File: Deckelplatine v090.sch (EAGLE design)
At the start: 67 parts, among them IC1 MAX1487EESA+, IC2 74HCT595D, IC3 74HCT595D, IC4 74HCT595D, IC5 74HCT595D, IC6 74HCT595D, J1 52808-2570, Q1 BC846BSMD, Q2 BC846BSMD, U1 LM2676S, X1 236-404, X2 233-502

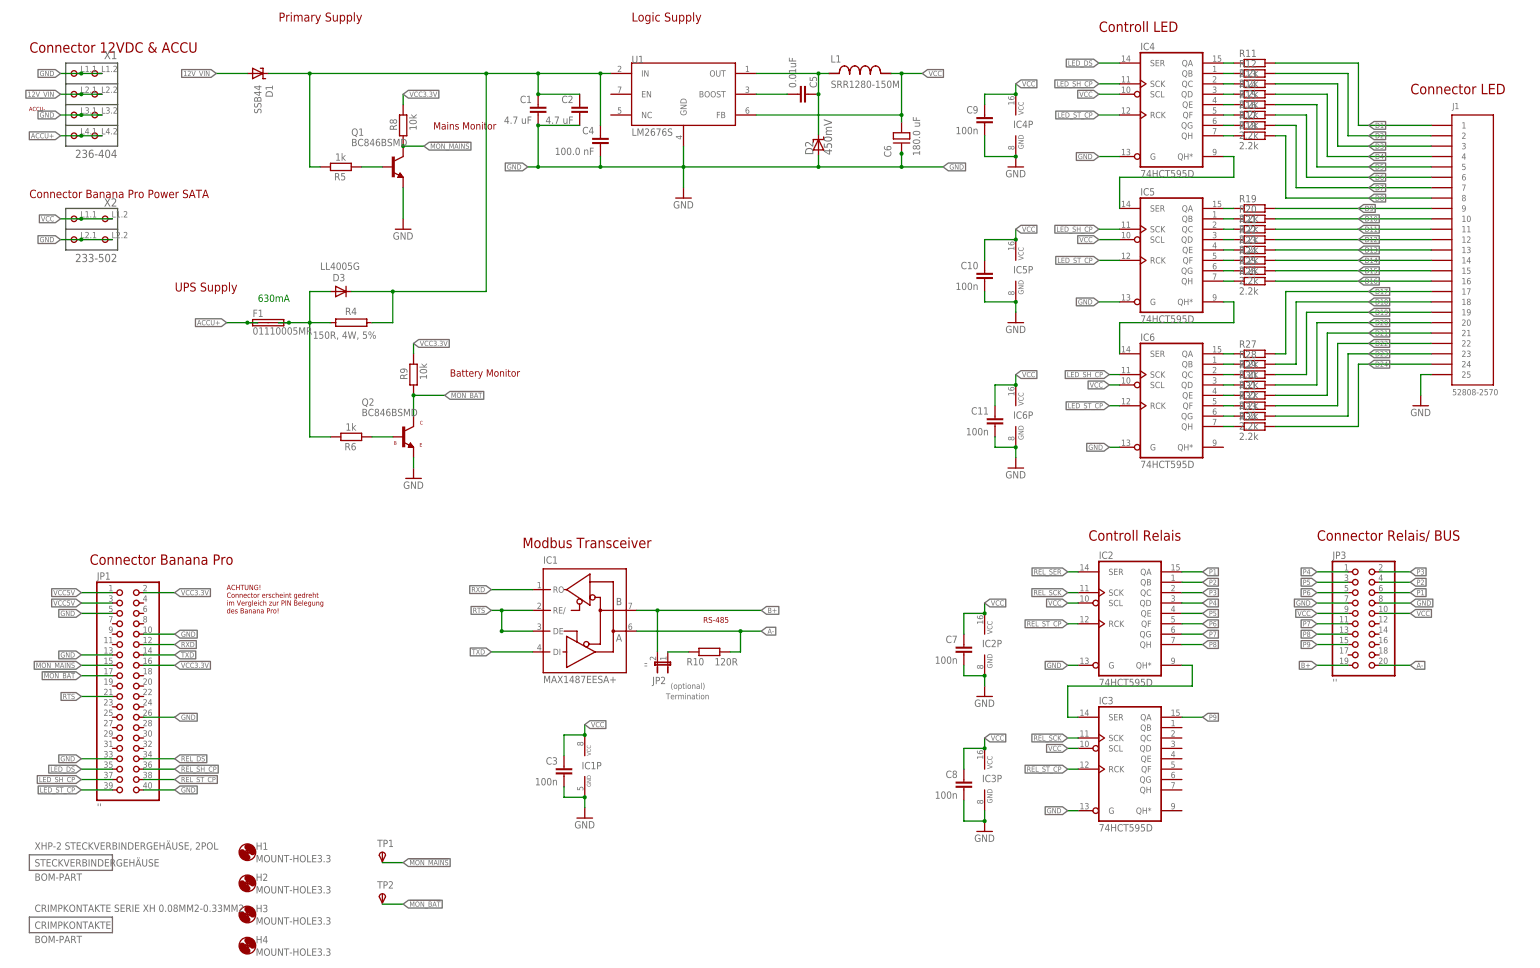
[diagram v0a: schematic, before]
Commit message: Erste Version in der PCB Produktion (Conrad)
Dies ist die erste Produktion die über https://www.leiterplattenservice.com/
abgewickelt wurde.

https://www.leiterplattenservice.com/code/my_orderhistory_details.html?nr=CR558950f00063a

Details:
-------
Nachfolgend sehen Sie die Details der gewählten Bestellung CR558950f00063a. Die Bestellung erfolgte am 23.06.2015, 14:28:32.
Anzahl 	Beschreibung 	Netto
EUR 	Brutto
EUR
2 	PCB-POOL Prototyp doppelseitig 	134.50 	160.06

    Länge in mm: 75
    Breite in mm: 110
    Dateiname: xMZ_Mod_Touch_Deckelplatine_v0...
    Dateiformat: EAGLE
    Lieferzeit: 8 Arbeitstage (AT)
    Basismaterial: FR4, 35µmCu, 1,6mm
    Stopplack: ja
    Der Preis enthält die Kosten für den Stopplack in Höhe von 36.65 EUR
    Bestückungsdruck: ja, nur BS
    Der Preis enthält die Kosten für den Bestückungsdruck in Höhe von 18.32 EUR
    Oberfläche: chem. Nickel/Gold (ENIG) für superflache Pads
    Min. Leiterbahnstärke / -abstand: >= 0.125mm (5mil)
    Min. Bohrenddurchmesser: >= 0.2mm (8mil)
    Möchten Sie, dass wir Ihre Leiterplatte einem elektrischen Test unterziehen? ja
    Der Preis enthält die Kosten für den E-Test in Höhe von 25.87 EUR.

	Warenwert LEITERPLATTEN in EUR 	134.50 	160.06
	Versandkosten LEITERPLATTEN in EUR 	5.80 	6.90
	Gesamtsumme in EUR 	140.30 	166.96
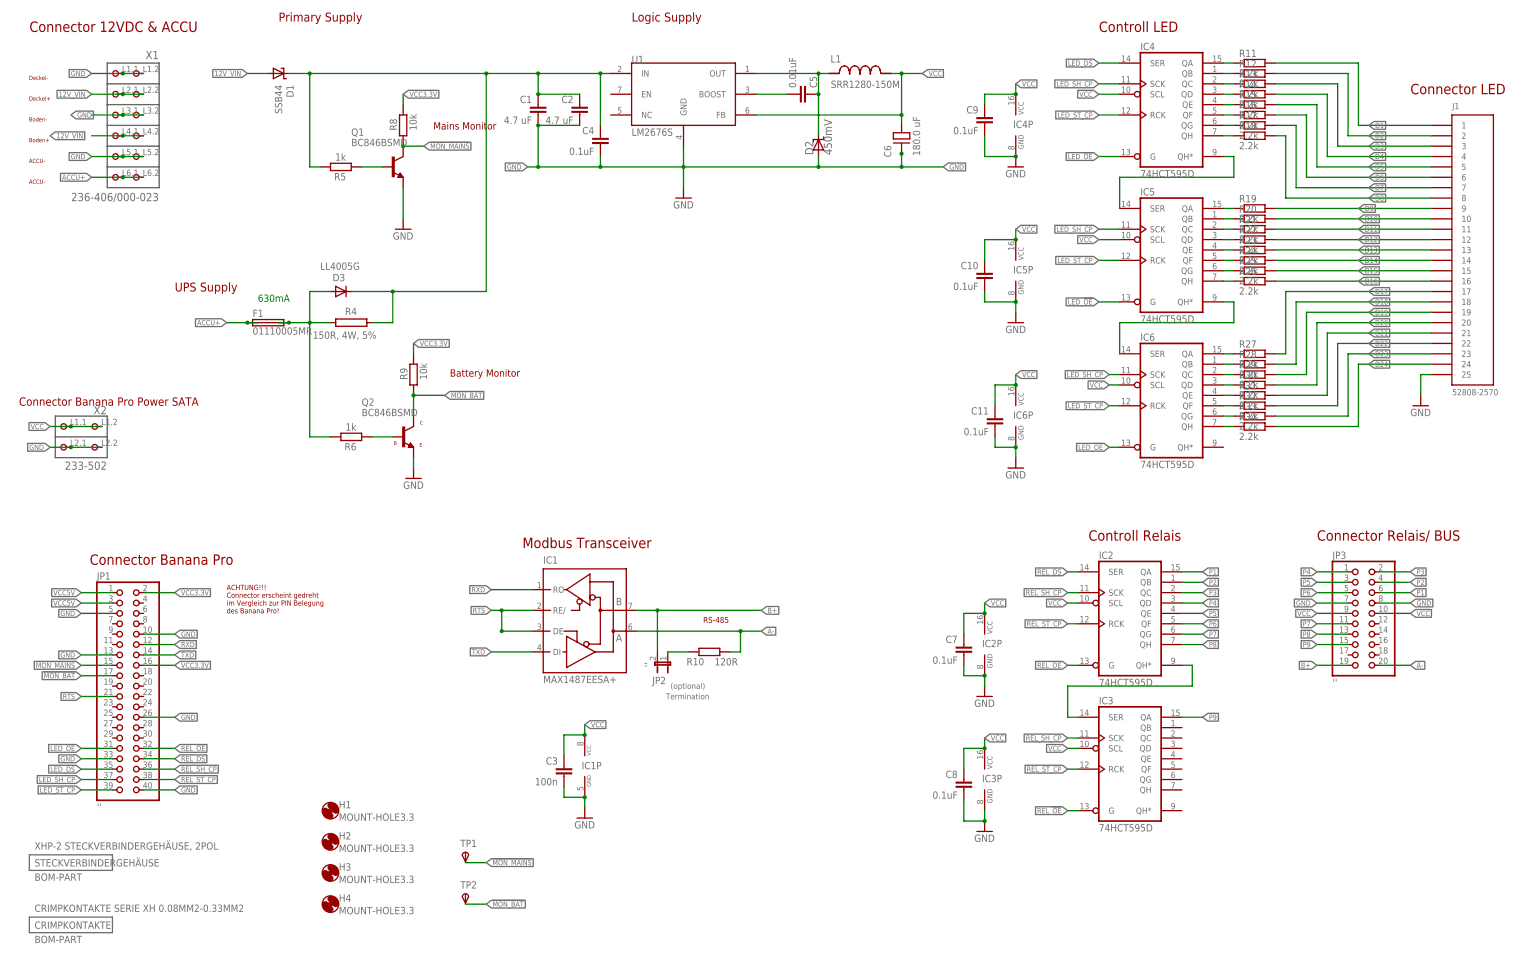
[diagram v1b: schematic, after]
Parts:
- C10, C11, C7, C8, C9: value 100n -> 0.1uF
- C4: value 100.0 nF -> 0.1uF
- X1: value 236-404 -> 236-406/000-023; device con-wago_236:236-404 -> con-wago_236:236-406/000-023; MPN 236-404 -> 236-406; OC_FARNELL 1283528 -> 1283529
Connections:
- removed net REL_SCK: IC2A.SCK, IC3A.SCK
- removed net REL_SER: IC2A.SER
- new net LED_!OE: IC4A.G, IC5A.G, IC6A.G, JP1.31
- new net REL_!OE: IC2A.G, IC3A.G, JP1.32
- net 12V_VIN: now also X1.P4.1, X1.P4.2
- net ACCU+: now also X1.P6.1, X1.P6.2; no longer X1.P4.1, X1.P4.2
- net GND: now also X1.P5.1, X1.P5.2; no longer IC2A.G, IC3A.G, IC4A.G, IC5A.G, IC6A.G
- net REL_DS: now also IC2A.SER
- net REL_SH_CP: now also IC2A.SCK, IC3A.SCK
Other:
- note added: "ACHTUNG!!! Connector erscheint gedreht im Vergleich zur PIN Belegung des Banana Pro!"
- note added: "Boden+"
- note added: "Boden-"
- note added: "Deckel+"
- note added: "Deckel-"
- note removed: "ACHTUNG! Connector erscheint gedreht im Vergleich zur PIN Belegung des Banana Pro!"
- moved on the sheet: D1, H1, H2, H3, H4, TP1, TP2, X2
